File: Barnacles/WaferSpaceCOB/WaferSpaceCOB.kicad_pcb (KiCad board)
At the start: 4 copper layers, 82.5 x 40 mm, 31 parts, among them J1 BOT_RAIL_POS, J12 Conn_02x03_Top_Bottom, J13 Conn_02x03_Top_Bottom, J2 TOP_RAIL_POS, J3 BOT_RAIL_NEG, J4 TOP_RAIL_NEG, J5 CENTER, J6 LED_GND

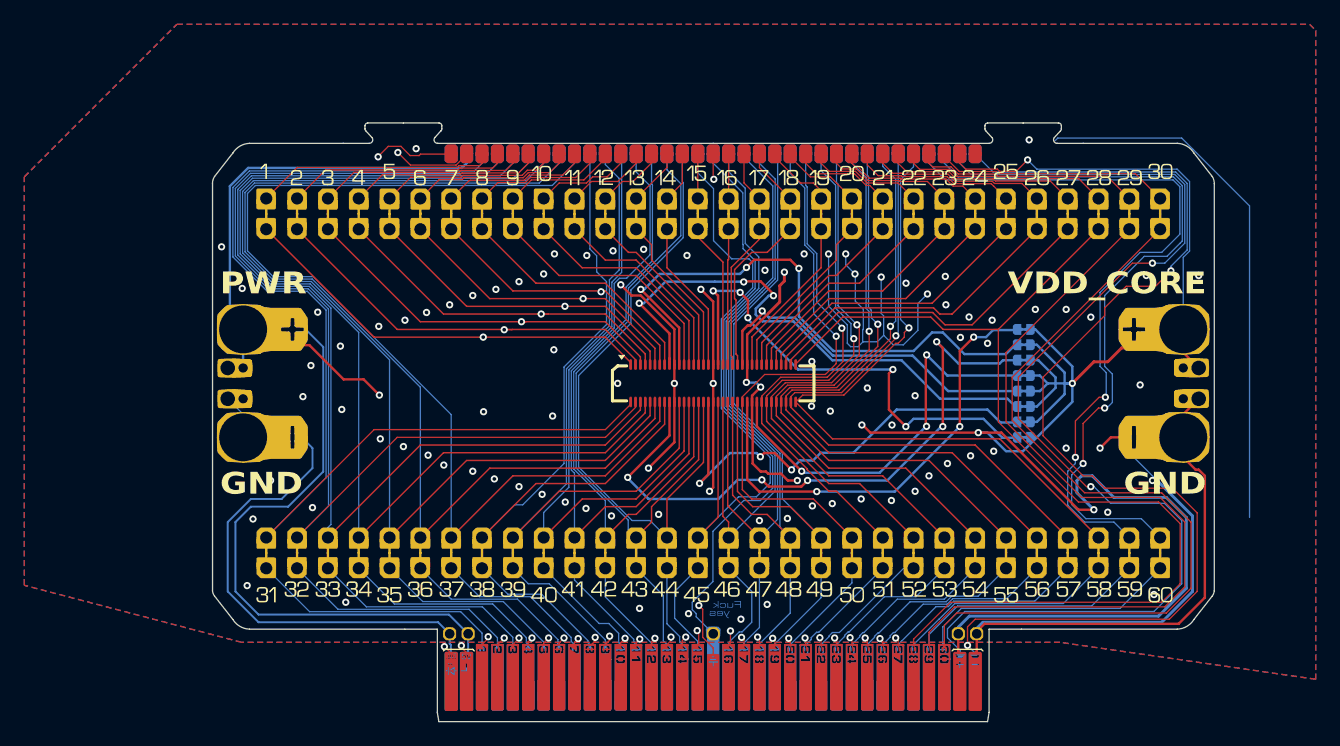
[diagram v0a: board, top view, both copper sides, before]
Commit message: add wigs
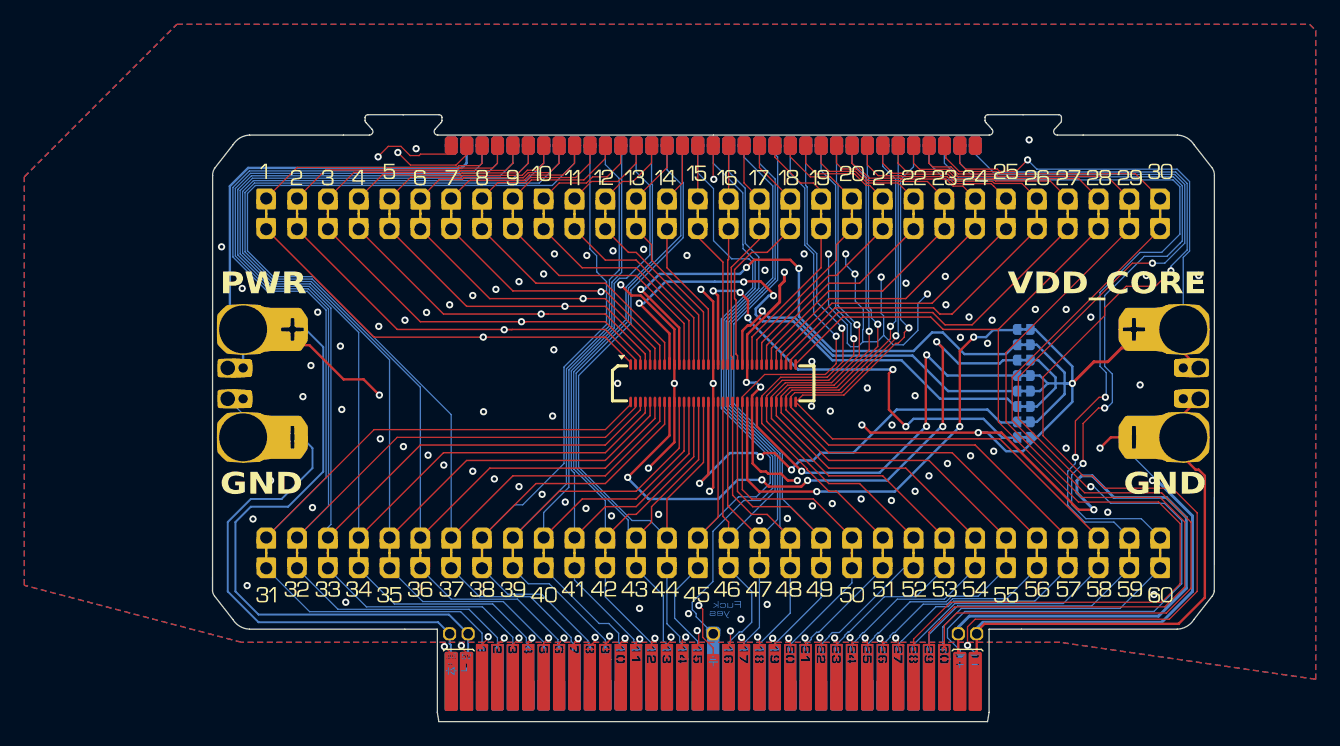
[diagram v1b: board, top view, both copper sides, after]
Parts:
- moved U3 0.68 mm to (185.7, 28.0)
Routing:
- net (no net): track 44.1 -> 0.00 mm
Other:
- board size 82.5 x 40 mm -> 82.6 x 40.7 mm
